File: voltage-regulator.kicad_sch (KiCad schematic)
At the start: 15 parts, among them J1 PWR, J2 PWR, U1 AMS1117-3.3

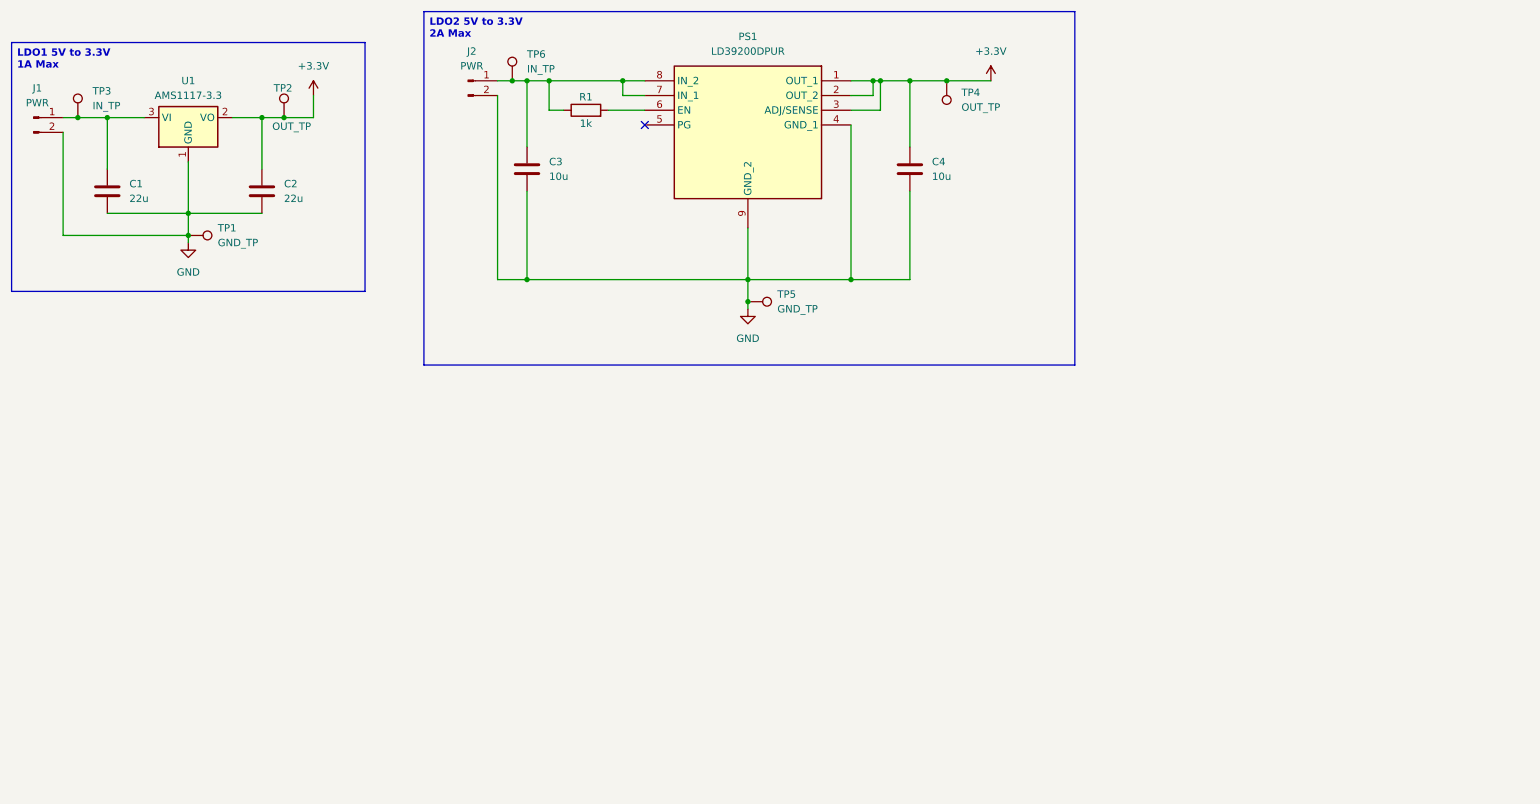
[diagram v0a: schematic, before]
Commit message: Added switching regulator
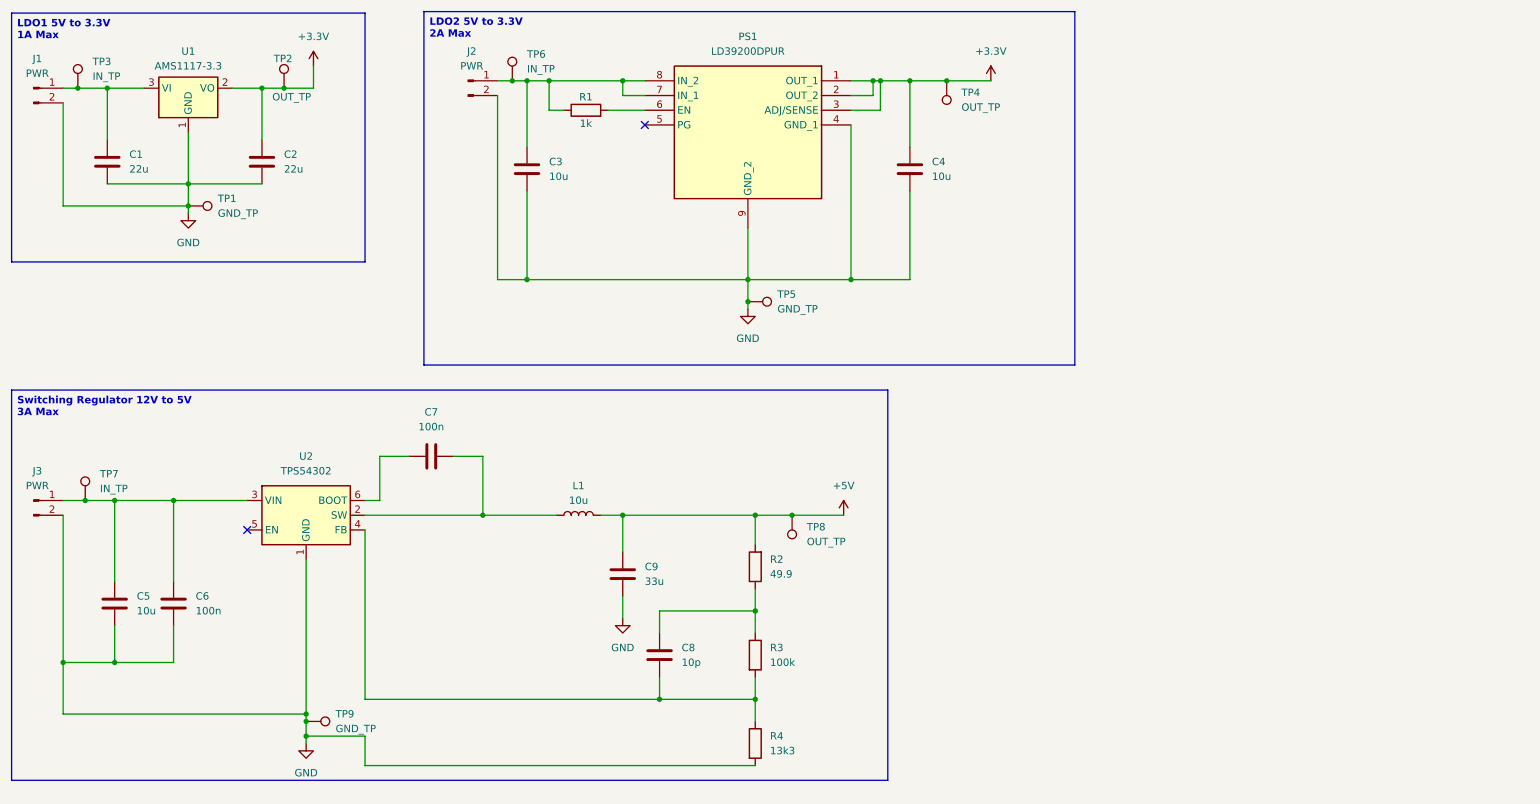
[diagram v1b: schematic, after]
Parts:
- added C5: 10u, symbol Device:C
- added C6, C7: 100n, symbol Device:C
- added C8: 10p, symbol Device:C
- added C9: 33u, symbol Device:C
- added J3: PWR, symbol Connector:Conn_01x02_Pin
- added L1: 10u, symbol Device:L
- added R2: 49.9, symbol Device:R
- added R3: 100k, symbol Device:R
- added R4: 13k3, symbol Device:R
- added TP7: IN_TP, symbol Connector:TestPoint
- added TP8: OUT_TP, symbol Connector:TestPoint
- added TP9: GND_TP, symbol Connector:TestPoint
- added U2: TPS54302, Package_TO_SOT_SMD:SOT-23-6, symbol Regulator_Switching:TPS54302
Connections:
- net GND: now also C5.2, C6.2, C9.1, J3.2 (Pin_2), R4.2, TP9.1, U2.1 (GND)
- new net: C8.1, R2.1, R3.1
- new net: C8.2, R3.2, R4.1, U2.4 (FB)
- new net: C5.1, C6.1, J3.1 (Pin_1), TP7.1, U2.3 (VIN)
- new net: C7.2, L1.1, U2.2 (SW)
- new net: C7.1, U2.6 (BOOT)
- new net +5V: C9.2, L1.2, R2.2, TP8.1
- no-connect marks 1 -> 2
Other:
- moved on the sheet: C1, C2, J1, TP1, TP2, TP3, U1

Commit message: Added changes
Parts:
- removed PS1: LD39200DPUR, SON80P400X400X100-9N-D, symbol LD39200DPUR:LD39200DPUR
- removed TP3, TP6, TP7: IN_TP, symbol Connector:TestPoint
- added D1: PRW_LED, LED_SMD:LED_0603_1608Metric, symbol Device:LED
- added D2, D3: PWR_LED, LED_SMD:LED_0603_1608Metric, symbol Device:LED
- added PS2: LD39200DPUR, SamacSys_Parts:SON80P400X400X100-9N-D, symbol SamacSys_Parts:LD39200DPUR
- added R5, R6, R7: 1k5, Resistor_SMD:R_0402_1005Metric, symbol Device:R
- C1, C2, C9: footprint (none) -> Capacitor_SMD:C_0805_2012Metric
- C3, C4, C5: footprint (none) -> Capacitor_SMD:C_0603_1608Metric
- C6, C7, C8: footprint (none) -> Capacitor_SMD:C_0402_1005Metric
- J1, J2, J3: footprint (none) -> Connector_PinHeader_2.54mm:PinHeader_1x02_P2.54mm_Vertical
- L1: footprint (none) -> Inductor_SMD:L_0805_2012Metric
- R1, R4: footprint (none) -> Resistor_SMD:R_0402_1005Metric
- R2: footprint (none) -> Resistor_SMD:R_0201_0603Metric
- R3: footprint (none) -> Resistor_SMD:R_0603_1608Metric
- TP1, TP2, TP4, TP5, TP8, TP9: footprint (none) -> Connector_Pin:Pin_D1.0mm_L10.0mm
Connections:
- net +3.3V: now also D1.2 (A), D2.2 (A), PS2.1 (OUT_1), PS2.2 (OUT_2), PS2.3 (ADJ/SENSE)
- net +5V: now also D3.2 (A)
- net GND: now also PS2.4 (GND_1), PS2.9 (GND_2), R5.2, R6.2, R7.2
- net FB: now reaches C8.2, R3.2, R4.1, U2.4 (FB)
- net V_IN1: now reaches C3.2, J2.1 (Pin_1), R1.1
- net V_IN1: now also PS2.7 (IN_1), PS2.8 (IN_2)
- net VIN: now reaches C5.1, C6.1, J3.1 (Pin_1), U2.3 (VIN)
- net VI: now reaches C1.2, J1.1 (Pin_1), U1.3 (VI)
- net SW: now reaches C7.2, L1.1, U2.2 (SW)
- net EN: now reaches R1.2
- net EN: now also PS2.6 (EN)
- net BOOT: now reaches C7.1, U2.6 (BOOT)
- new net: D3.1 (K), R7.1
- new net: D1.1 (K), R5.1
- new net: D2.1 (K), R6.1
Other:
- moved on the sheet: C3, C4, J2, R1, TP4, TP5

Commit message: Added changes
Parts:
- added H1, H2, H3, H4: MountingHole, MountingHole:MountingHole_2.2mm_M2, symbol Mechanical:MountingHole
- L1: footprint Inductor_SMD:L_0805_2012Metric -> SamacSys_Parts:INDPM6965X300N
- R2: footprint Resistor_SMD:R_0201_0603Metric -> Resistor_SMD:R_0402_1005Metric
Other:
- note added: "Use M2-size"
